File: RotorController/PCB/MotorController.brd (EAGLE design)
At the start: 100 x 80 mm, 18 parts

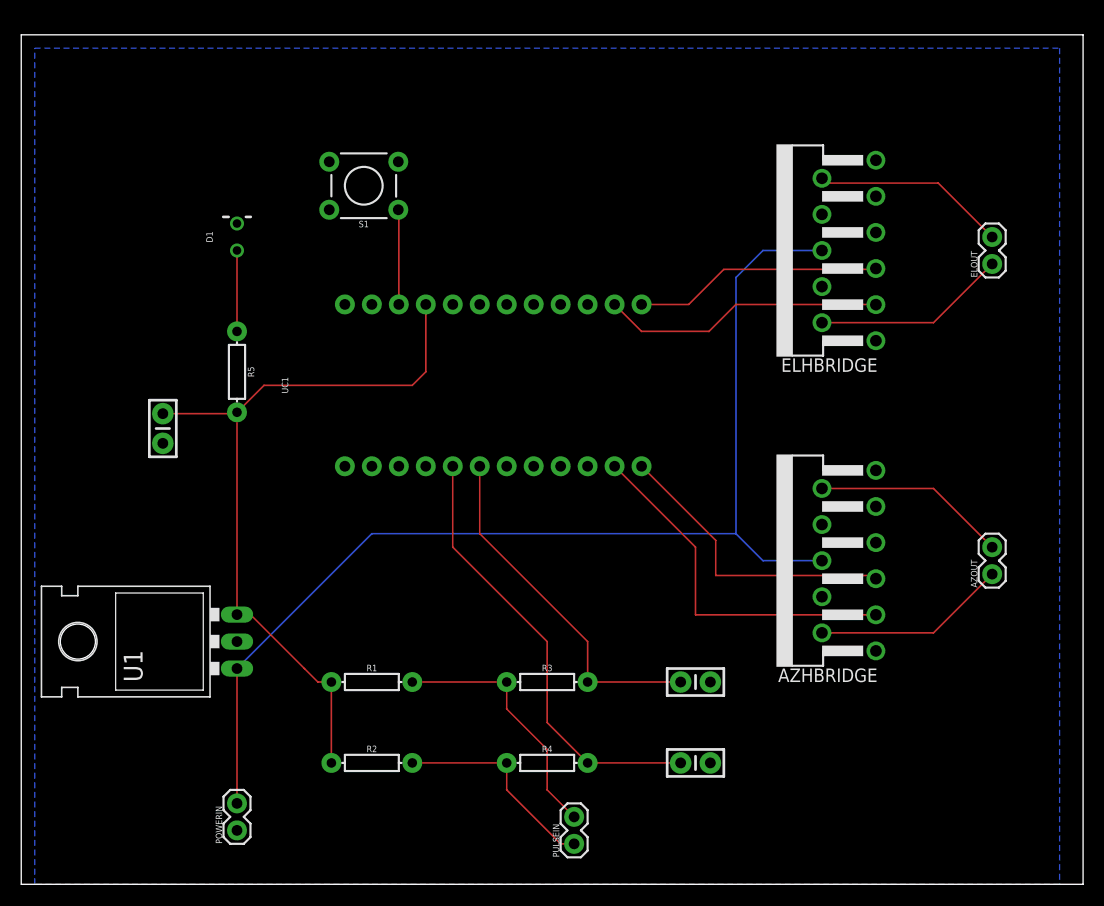
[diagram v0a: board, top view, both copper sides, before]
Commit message: Added thermal warning logic and fixed some layout issues.
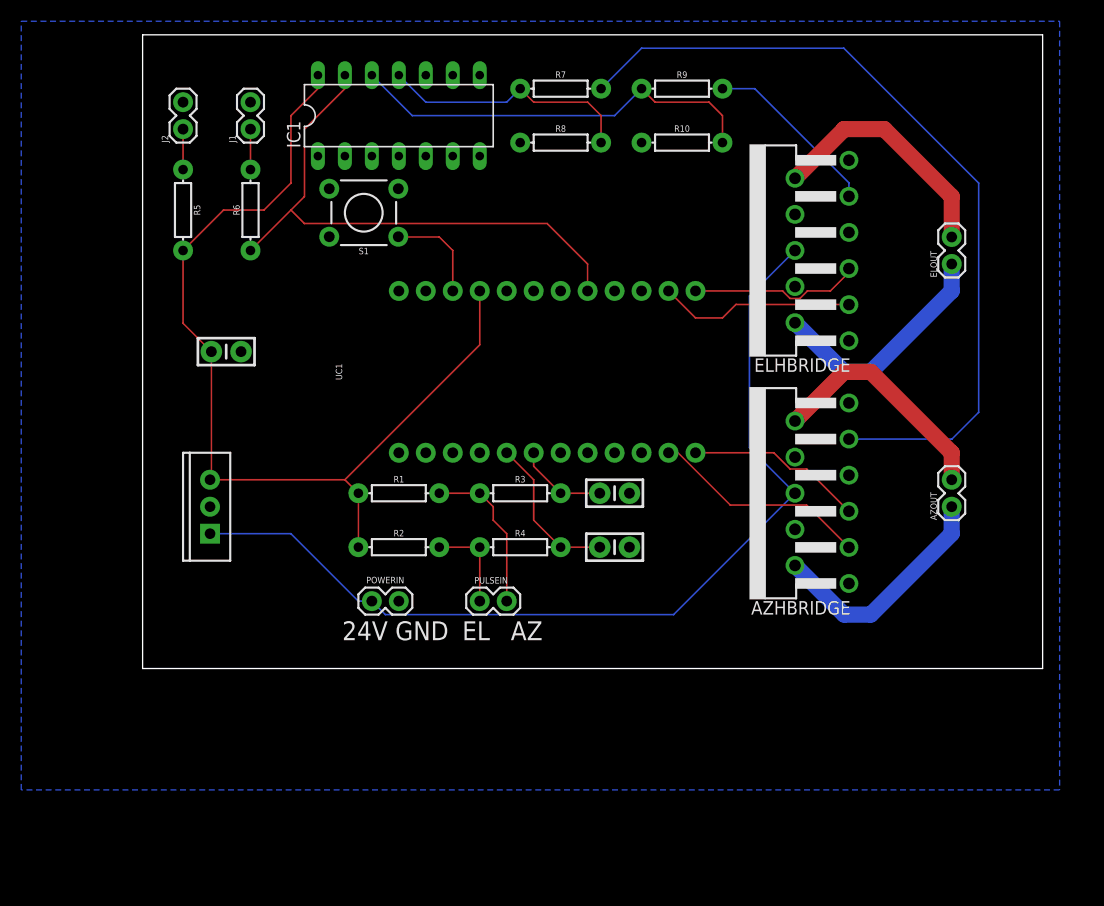
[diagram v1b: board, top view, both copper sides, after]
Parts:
- removed D1: (no value), SparkFun-LED:LED_3MM-NS
- removed U1: (no value), SparkFun-IC-Power:TO-220-ALT
- added IC1: 74ALS02N, 74xx-us:DIL14
- added J1: Waring LED, SparkFun-Connectors:1X02
- added J2: Power LED, SparkFun-Connectors:1X02
- added R10, R8: 2.2K, SparkFun-Resistors:AXIAL-0.3
- added R6: 1K, SparkFun-Resistors:AXIAL-0.3
- added R7, R9: 3.3K, SparkFun-Resistors:AXIAL-0.3
- added U2: 5V, SparkFun-IC-Power:TO220-IGO
- moved POWERIN 26.4 mm to (35.6, 26.7), turned to 180 degrees
- moved PULSEIN 24.5 mm to (43.2, 26.7), turned to 0 degrees
- moved C3 21.7 mm to (55.9, 31.8)
- moved R2 20.5 mm to (35.6, 31.8)
- moved R4 20.5 mm to (47.0, 31.8)
- moved C2 19.3 mm to (55.9, 36.8)
- moved R1 18.0 mm to (35.6, 36.8)
- moved R3 18.0 mm to (47.0, 36.8)
- moved R5 16.1 mm to (15.2, 63.5)
- moved C1 9.38 mm to (19.3, 50.2), turned to 0 degrees
- moved AZOUT 7.41 mm to (87.6, 35.6)
- moved AZHBRIDGE 6.84 mm to (68.6, 36.8)
- moved UC1 5.24 mm to (48.3, 48.3)
- moved ELOUT 3.81 mm to (87.6, 58.4)
- moved ELHBRIDGE 2.54 mm to (68.6, 59.7)
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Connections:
- new net AZFLAG: AZHBRIDGE.9, R7.P$2
- new net ELFLAG: ELHBRIDGE.9, R9.P$2
- new net N$3: IC1.12, R10.P$2, R9.P$1
- new net N$5: J1.1, R6.P$2
- new net N$7: IC1.11, R7.P$1, R8.P$2
- new net WARNINGFLAG: IC1.13, R6.P$1, UC1.17
- net GND: now also IC1.2, IC1.3, IC1.5, IC1.6, IC1.7, IC1.8, IC1.9, J1.2, J2.2, R10.P$1, R8.P$1, U2.GND; no longer D1.K, U1.GND
- net N$8: now also J2.1; no longer D1.A
- net VCC: now also IC1.14, U2.OUT; no longer U1.OUT
- net VCC_2: now also U2.IN; no longer U1.IN
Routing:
- net AZFLAG: track 0.00 -> 77.3 mm
- net WARNINGFLAG: track 0.00 -> 52.8 mm
- net N$3: track 0.00 -> 39.2 mm
- net ELPULSE: track 42.0 -> 14.7 mm
- net AZPULSE: track 33.3 -> 8.55 mm
- net N$7: track 0.00 -> 24.2 mm
- net VCC: track 70.9 -> 89.4 mm
- net VCC_2: track 107.4 -> 89.4 mm
- net ELFLAG: track 0.00 -> 16.9 mm
- net AZDIR: track 34.1 -> 20.7 mm
- net AZPWM: track 28.4 -> 16.7 mm
- net N$4: track 19.9 -> 8.89 mm
- net N$2: track 24.2 -> 15.0 mm
- net ELDIR: track 26.7 -> 18.6 mm
- net ELPWM: track 23.5 -> 16.1 mm
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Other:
- board size 100 x 80 mm -> 84.8 x 59.7 mm
- board text added: "24V GND"
- board text added: "AZ"
- board text added: "EL"
- board text added: "SRT Motor Controller Nathan Thomas thomasns@etsu.edu V0.01"

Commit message: Fixed PCB files with accurate footprints for passive components. Included gerber files. Updated the arduino project layout.
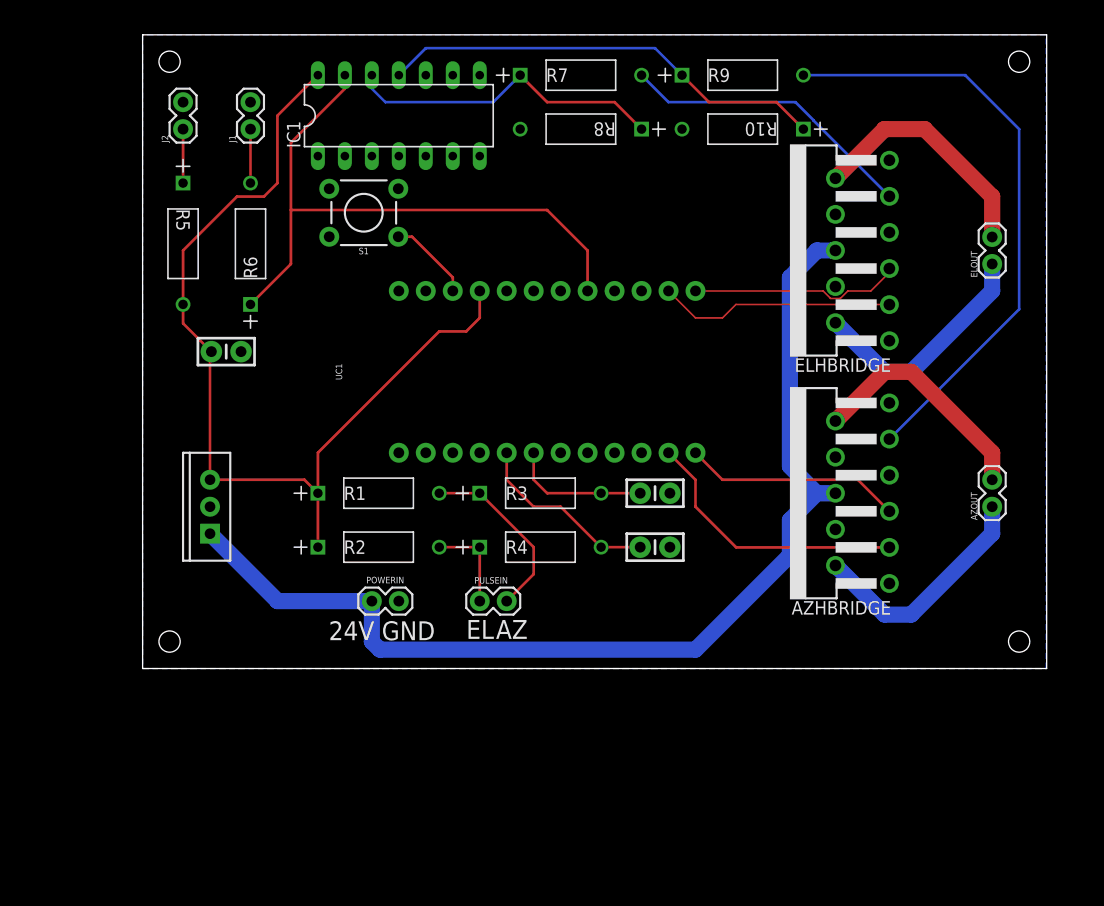
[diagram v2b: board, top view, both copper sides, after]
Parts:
- R1, R2, R5, R6: value 1K -> CF14JT1K00; device SparkFun-Resistors:AXIAL-0.3 -> DigiKeyImports:STA_CF14
- R10, R8: value 2.2K -> CF14JT2K20; device SparkFun-Resistors:AXIAL-0.3 -> DigiKeyImports:STA_CF14
- R3, R4: value 5.1K -> CF14JT5K50; device SparkFun-Resistors:AXIAL-0.3 -> DigiKeyImports:STA_CF14
- R7, R9: value 3.3K -> CF14JT3K30; device SparkFun-Resistors:AXIAL-0.3 -> DigiKeyImports:STA_CF14
- moved R9 11.5 mm to (73.7, 76.2)
- moved R5 8.89 mm to (15.2, 54.6)
- moved R7 7.73 mm to (58.4, 76.2)
- moved R3 7.62 mm to (54.6, 36.8)
- moved R4 7.62 mm to (54.6, 31.8)
- moved R8 4.02 mm to (47.0, 71.1), turned to 180 degrees
- moved AZHBRIDGE 3.81 mm to (72.4, 36.8)
- moved AZOUT 3.81 mm to (91.4, 35.6)
- moved ELHBRIDGE 3.81 mm to (72.4, 59.7)
- moved ELOUT 3.81 mm to (91.4, 58.4)
- moved C2 3.81 mm to (59.7, 36.8)
- moved C3 3.81 mm to (59.7, 31.8)
- moved R1 3.81 mm to (39.4, 36.8)
- moved R2 3.81 mm to (39.4, 31.8)
- moved R6 2.54 mm to (21.6, 66.0)
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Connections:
- removed net N$7: IC1.11, R7.P$1, R8.P$2
- new net N$9: IC1.11, R10.1, R9.1
- net AZFLAG: now also R9.2; no longer R7.P$2
- net AZPULSE: now also R3.2; no longer R3.P$2
- net ELFLAG: now also R7.2; no longer R9.P$2
- net ELPULSE: now also R4.2; no longer R4.P$2
- net GND: now also R10.2, R8.2; no longer R10.P$1, R8.P$1
- net N$2: now also R1.2, R3.1; no longer R1.P$2, R3.P$1
- net N$3: now also R7.1, R8.1; no longer R10.P$2, R9.P$1
- net N$4: now also R2.2, R4.1; no longer R2.P$2, R4.P$1
- net N$5: now also R6.2; no longer R6.P$2
- net N$8: now also R5.1; no longer R5.P$1
- net VCC: now also R1.1, R2.1, R5.2; no longer R1.P$1, R2.P$1, R5.P$2
- net WARNINGFLAG: now also R6.1; no longer R6.P$1
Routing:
- net N$9: track 0.00 -> 42.3 mm
- net N$7: track 24.2 -> 0.00 mm
- net AZFLAG: track 77.3 -> 56.7 mm
- net ELFLAG: track 16.9 -> 28.1 mm
- net VCC_2: track 89.4 -> 100.4 mm
- net N$3: track 39.2 -> 30.4 mm
- net WARNINGFLAG: track 52.8 -> 58.6 mm
- net AZDIR: track 20.7 -> 26.0 mm
- net AZPULSE: track 8.55 -> 13.1 mm
- net ELPWM: track 16.1 -> 19.9 mm
- net AZPWM: track 16.7 -> 20.5 mm
- net ELDIR: track 18.6 -> 22.4 mm
- net ELPULSE: track 14.7 -> 17.7 mm
- net N$2: track 15.0 -> 17.1 mm
- net N$1: track 9.48 -> 7.99 mm
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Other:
- board size 84.8 x 59.7 mm -> 85.1 x 59.7 mm
- board text added: "SRT Motor Controller Rev. 2 Nathan Thomas thomasns@etsu.edu"
- board text removed: "SRT Motor Controller Nathan Thomas thomasns@etsu.edu V0.01"
